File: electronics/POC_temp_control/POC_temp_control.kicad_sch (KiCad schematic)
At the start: 177 parts, among them J1 Conn_01x02, J2 Conn_01x07, J3 Conn_01x05, J4 Conn_01x06, J5 Conn_01x02, J6 Conn_01x02, Q1 PXT8050, Q2 PXT8050, Q3 PXT8550, Q4 Q_PMOS_DUAL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

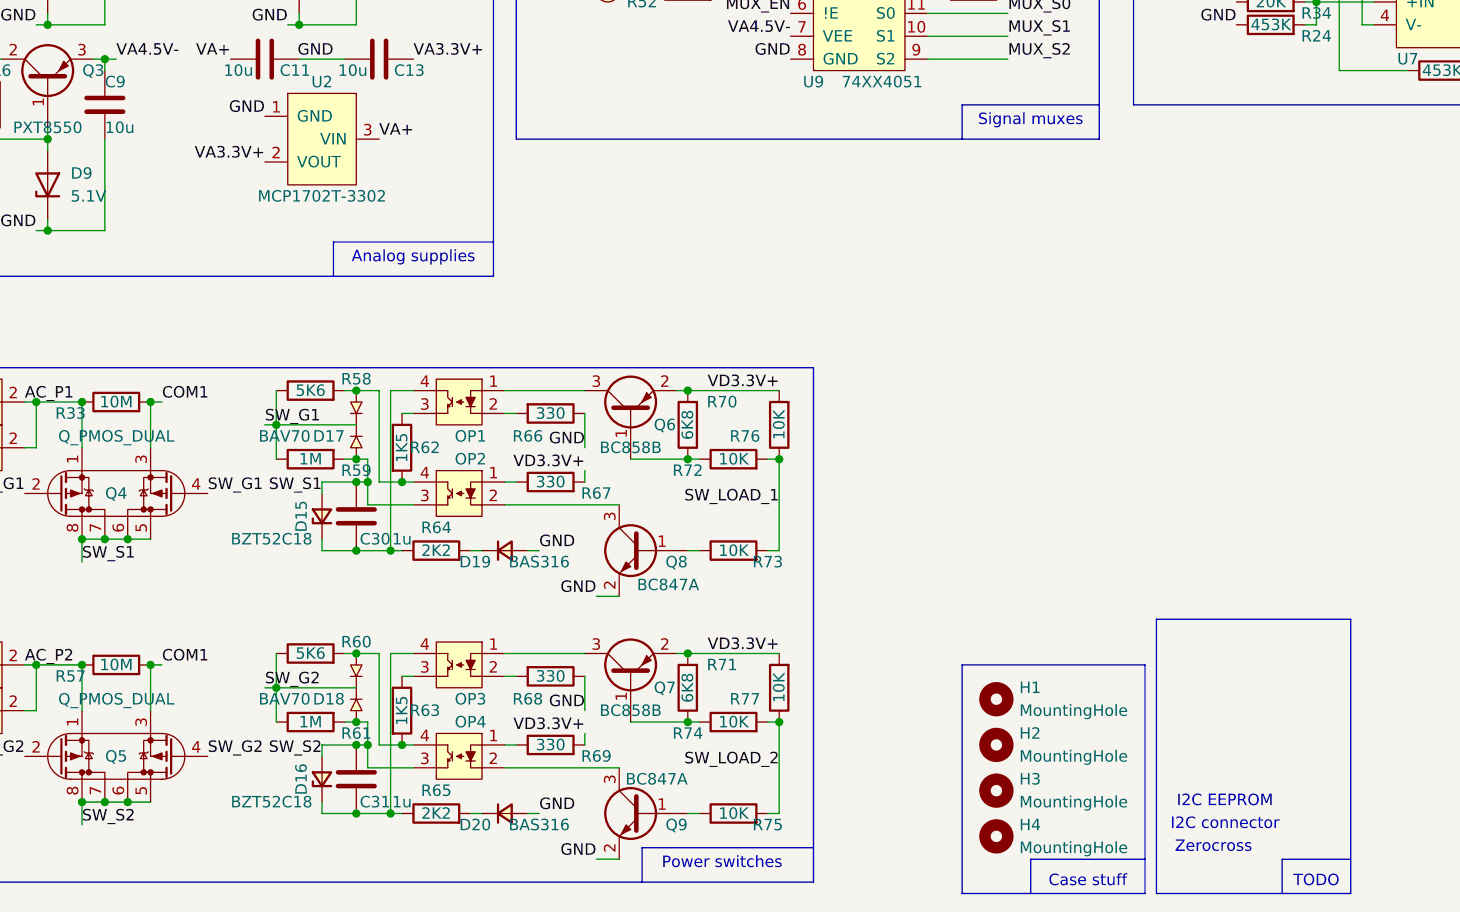
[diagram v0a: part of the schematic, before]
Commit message: added zerocross detector schematic
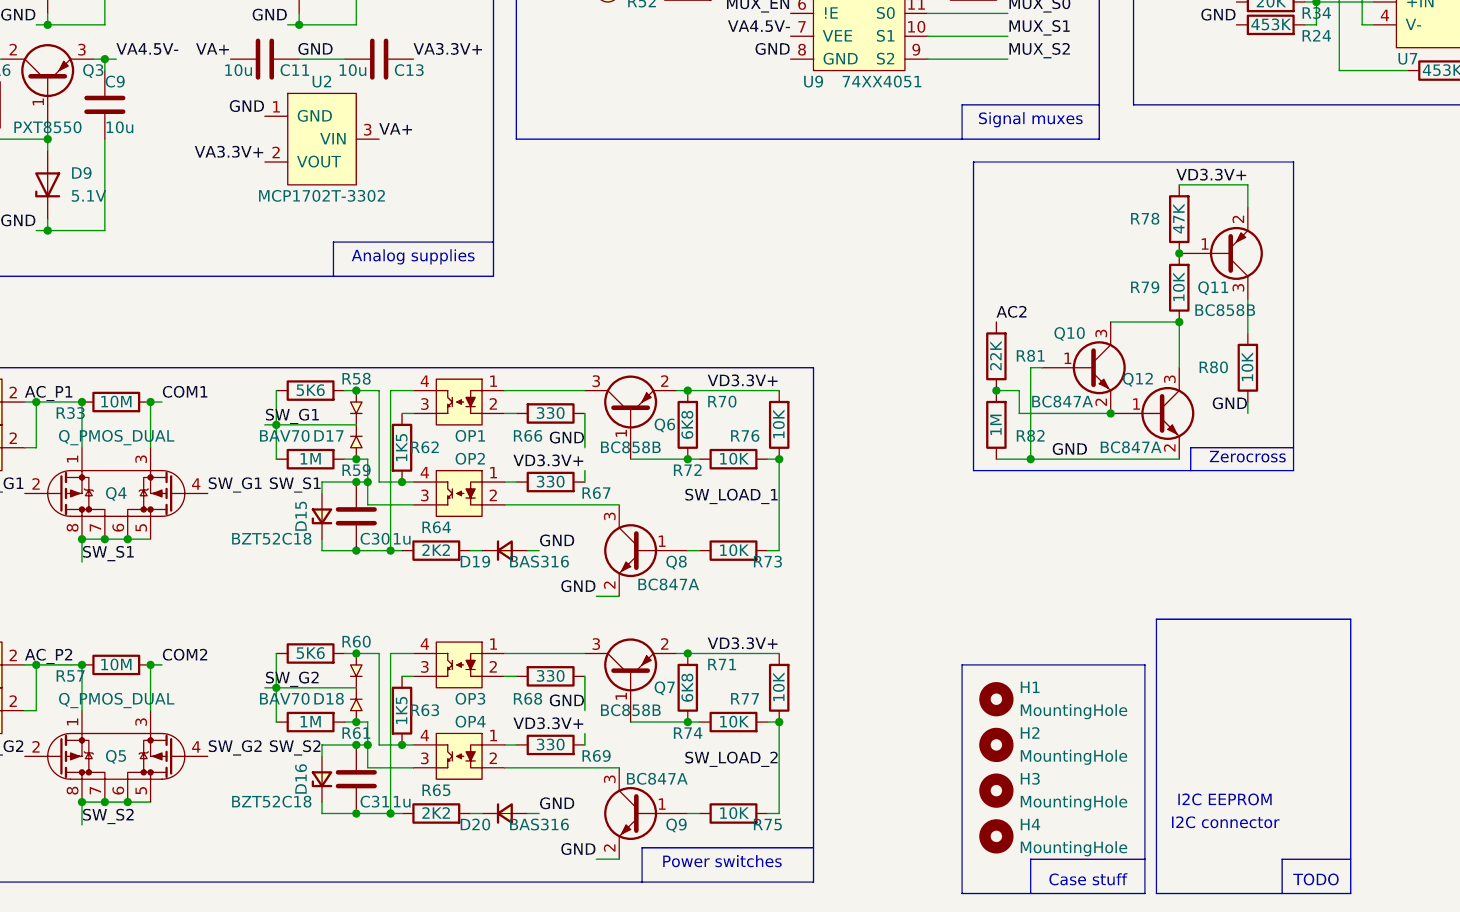
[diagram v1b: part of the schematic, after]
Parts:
- added Q10, Q12: BC847A, SquantorIC:SOT23-3, symbol Device:Q_NPN_BEC
- added Q11: BC858B, SquantorIC:SOT23-3, symbol Device:Q_PNP_BEC
- added R78: 47K, SquantorResistor:R_0603_hand, symbol Device:R
- added R79, R80: 10K, SquantorResistor:R_0603_hand, symbol Device:R
- added R81: 22K, SquantorResistor:R_0603_hand, symbol Device:R
- added R82: 1M, SquantorResistor:R_0603_hand, symbol Device:R
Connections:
- net AC2: now also R81.2
- net COM1: no longer Q5.3 (S2), R57.2
- net COM2: now also Q5.3 (S2), R57.2
- net GND: now also Q10.1 (B), Q12.2 (E), R80.1, R82.1
- net VD3.3V+: now also Q11.2 (E), R78.2
- new net: Q10.2 (E), Q12.1 (B), R81.1, R82.2
- new net: Q10.3 (C), Q12.3 (C), R79.1
- new net: Q11.3 (C), R80.2
- new net: Q11.1 (B), R78.1, R79.2

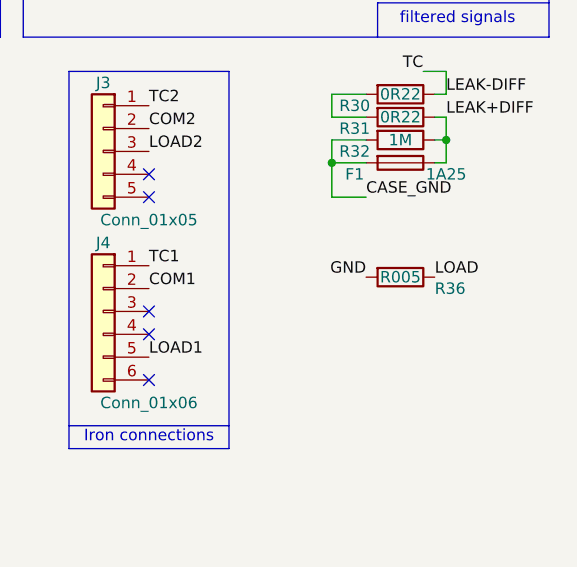
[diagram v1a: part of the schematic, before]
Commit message: replaced current sense resistor, imported zerocross detector
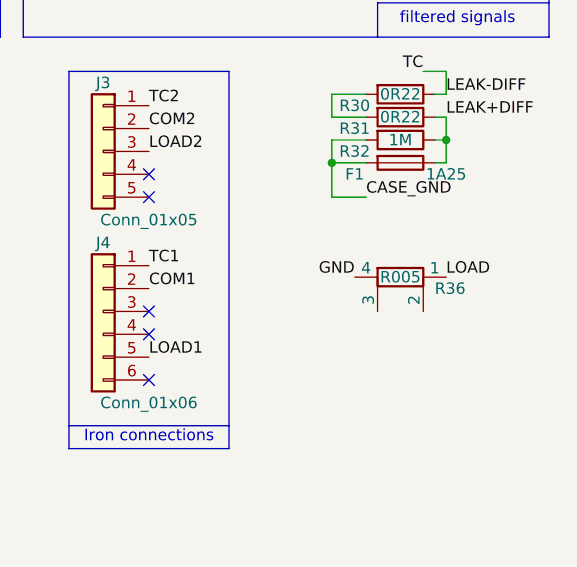
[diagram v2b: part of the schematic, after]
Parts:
- R36: footprint SquantorResistor:R_2512 -> SquantorResistor:R_1225_kelvin; symbol Device:R -> Device:R_Shunt
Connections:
- net GND: now also R36.4; no longer R36.2
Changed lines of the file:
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@@
 	)
 	(label "GND"
-		(at 262.89 135.89 180)
+		(at 261.62 135.89 180)
 		(fields_autoplaced yes)
 		(effects
@@
 	)
 	(label "LOAD"
-		(at 270.51 135.89 0)
+		(at 271.78 135.89 0)
 		(fields_autoplaced yes)
 		(effects
@@
 	)
 	(symbol
-		(lib_id "Device:R")
+		(lib_id "Device:R_Shunt")
 		(at 266.7 135.89 270)
 		(unit 1)
@@
 			)
 		)
-		(property "Footprint" "SquantorResistor:R_2512"
+		(property "Footprint" "SquantorResistor:R_1225_kelvin"
 			(at 266.7 134.112 90)
 			(effects
@@
 			)
 		)
-		(property "Description" "Resistor"
+		(property "Description" "Shunt resistor"
 			(at 266.7 135.89 0)
 			(effects
@@
 		(pin "2"
 		)
+		(pin "4"
+		)
+		(pin "3"
+		)
 		(instances

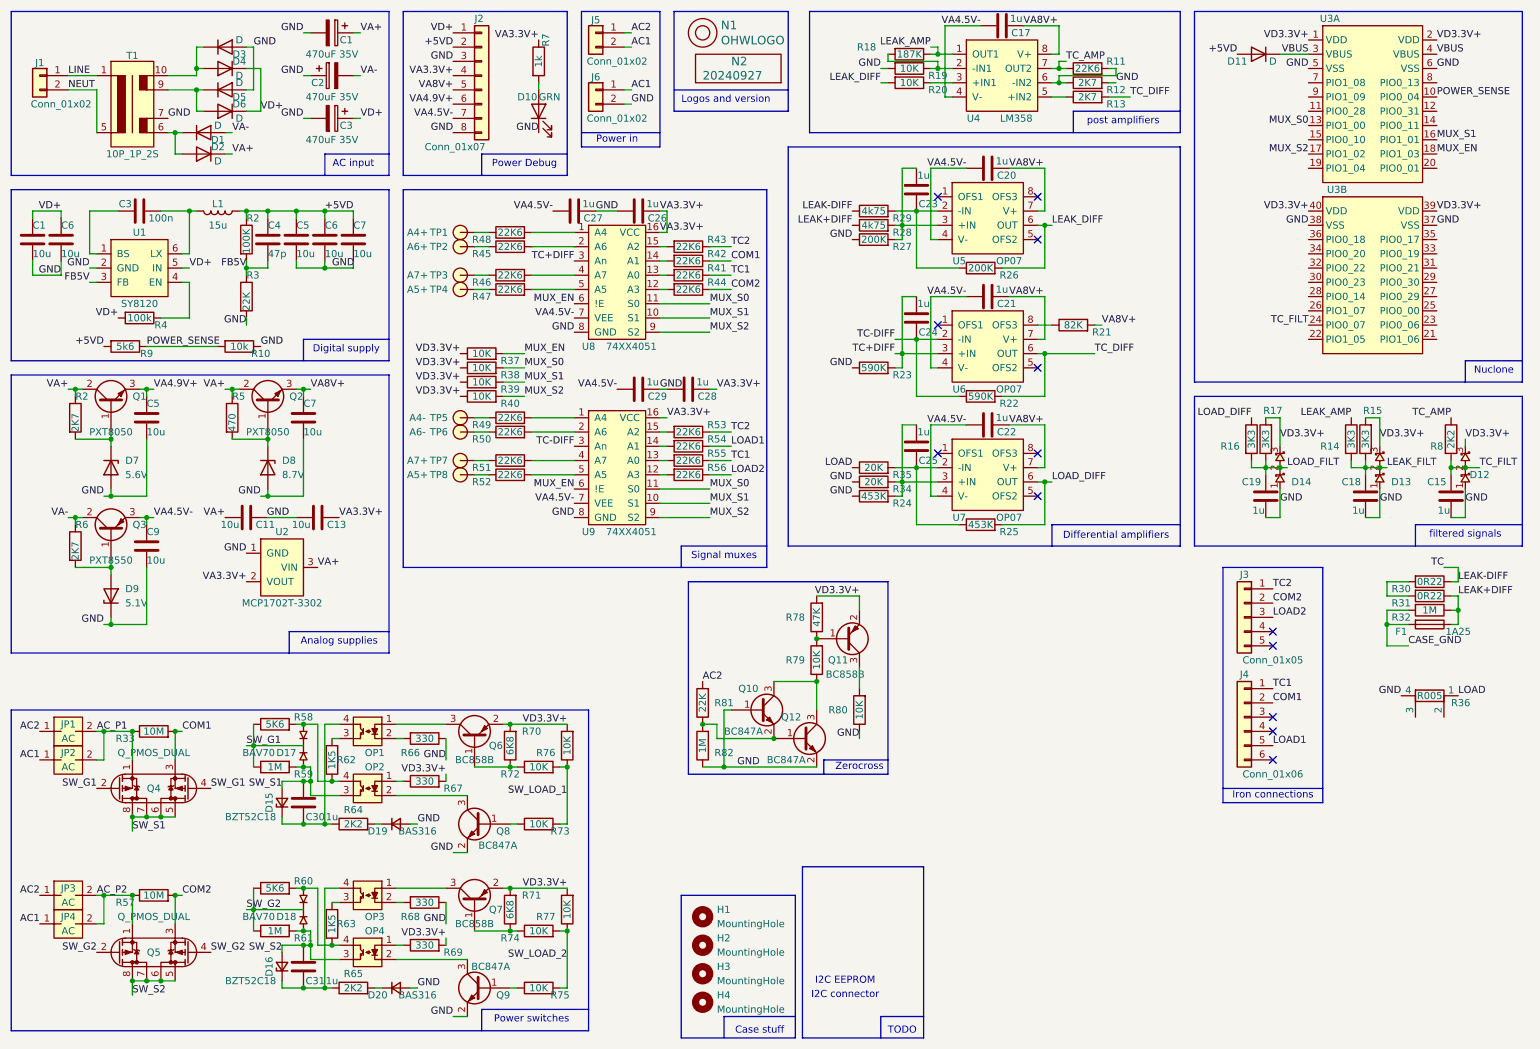
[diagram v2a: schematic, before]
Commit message: more schematic bits added, passes ERC, placing components and fixing silk orientations
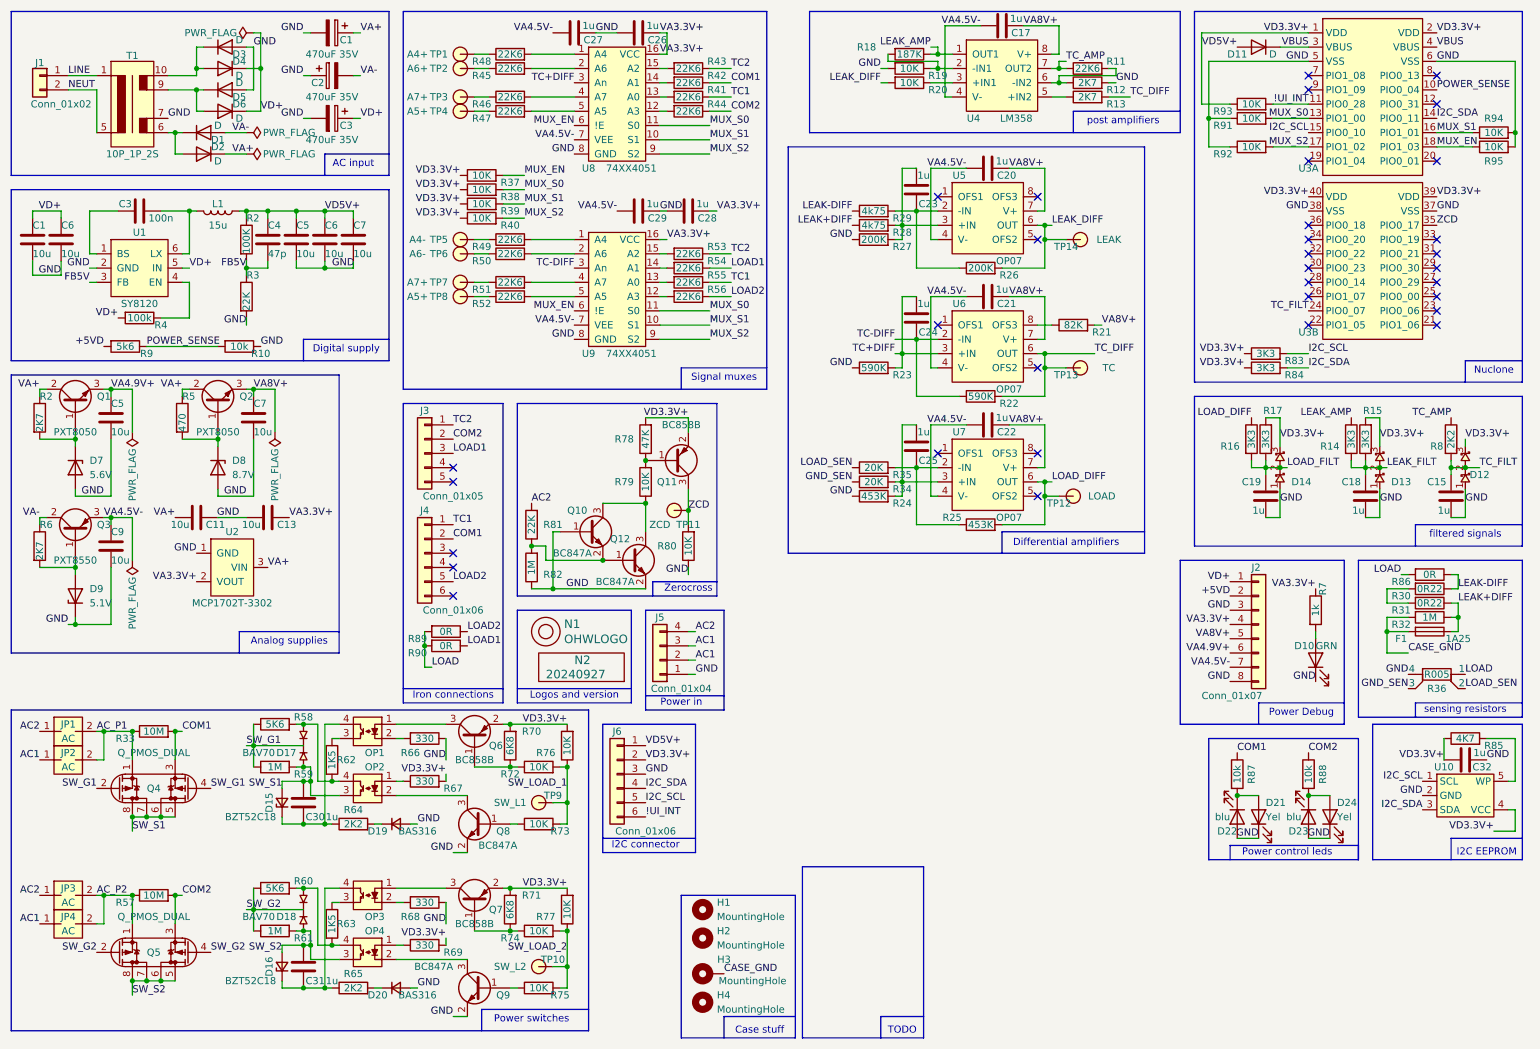
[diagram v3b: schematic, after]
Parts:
- removed J5, J6: Conn_01x02, SquantorPhoenixContact:MKDS_2conn_508pitch_1711725, symbol Connector_Generic:Conn_01x02
- added C32: 1u, SquantorCapacitor:C_0603, symbol Device:C
- added D21, D24: Yel, SquantorDiodes:LED_0603_hand, symbol Device:LED
- added D22, D23: blu, SquantorDiodes:LED_0603_hand, symbol Device:LED
- added J5: Conn_01x04, SquantorConnectors:phoenix-MSTBVA-1755752-4p-508-str, symbol Connector_Generic:Conn_01x04
- added J6: Conn_01x06, Connector_JST:JST_PH_B6B-PH-K_1x06_P2.00mm_Vertical, symbol Connector_Generic:Conn_01x06
- added R83, R84: 3K3, SquantorResistor:R_0603_hand, symbol Device:R
- added R85: 4K7, SquantorResistor:R_0603_hand, symbol Device:R
- added R86, R89, R90: 0R, SquantorResistor:R_1206, symbol Device:R
- added R87, R88: 10k, SquantorResistor:R_0603_hand, symbol Device:R
- added R91, R92, R93, R94, R95: 10K, SquantorResistor:R_0603_hand, symbol Device:R
- added TP10: SW_L2, SquantorTestPoints:TestPoint_hole_H05R10, symbol SquantorProto:testpad
- added TP11: ZCD, SquantorTestPoints:TestPoint_hole_H05R10, symbol SquantorProto:testpad
- added TP12: LOAD, SquantorTestPoints:TestPoint_hole_H05R10, symbol SquantorProto:testpad
- added TP13: TC, SquantorTestPoints:TestPoint_hole_H05R10, symbol SquantorProto:testpad
- added TP14: LEAK, SquantorTestPoints:TestPoint_hole_H05R10, symbol SquantorProto:testpad
- added TP9: SW_L1, SquantorTestPoints:TestPoint_hole_H05R10, symbol SquantorProto:testpad
- added U10: ~, SquantorIC:SOT23-5-Microchip-OT, symbol SquantorGenericDigital:EEPROM_SOT_I2C
- F1: footprint SquantorResistor:R_1206 -> SquantorFuse:FH_XF-155
- H3: symbol Mechanical:MountingHole -> Mechanical:MountingHole_Pad
- R30, R31: footprint SquantorResistor:R_0805+0603 -> SquantorResistor:R_1206
- R36: symbol Device:R_Shunt -> SquantorDevice:R_Shunt
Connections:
- net +5VD: no longer C4.1, C5.1, C6.1, C7.1, D11.2 (A), L1.1, R2.1
- net AC1: now also J5.2 (Pin_2), J5.3 (Pin_3)
- net AC2: now also J5.4 (Pin_4)
- net CASE_GND: now also H3.1
- net COM1: now also R87.1
- net COM2: now also R88.1
- net GND: now also C32.1, D21.1 (K), D22.2 (A), D23.2 (A), D24.1 (K), J5.1 (Pin_1), J6.3 (Pin_3), R91.1, R92.1, R94.2, R95.2, U10.2 (GND); no longer R34.1
- net LEAK-DIFF: now also R86.1
- net LEAK_DIFF: now also TP14.1
- net LOAD: now also R86.2, R89.2, R90.2; no longer R35.1
- net LOAD1: now also J3.3 (Pin_3), R90.1; no longer J4.5 (Pin_5)
- net LOAD2: now also J4.5 (Pin_5), R89.1; no longer J3.3 (Pin_3)
- net LOAD_DIFF: now also TP12.1
- net MUX_EN: now also R95.1
- net MUX_S0: now also R91.2
- net MUX_S1: now also R94.1
- net MUX_S2: now also R92.2
- net SW_LOAD_1: now also TP9.1
- net SW_LOAD_2: now also TP10.1
- net TC_DIFF: now also TP13.1
- net VD3.3V+: now also C32.2, J6.2 (Pin_2), R83.1, R84.1, R85.1, R93.1, U10.4 (VCC)
- net ZCD: now reaches Q11.3 (C), R80.2
- net ZCD: now also U3.35 (PIO0_17), TP11.1
- net !UI_INT: now reaches U3.11 (PIO0_28)
- net !UI_INT: now also J6.6 (Pin_6), R93.2
- net I2C_SDA: now reaches U3.14 (PIO0_11)
- net I2C_SDA: now also J6.4 (Pin_4), R84.2, U10.3 (SDA)
- net I2C_SCL: now reaches U3.15 (PIO0_10)
- net I2C_SCL: now also J6.5 (Pin_5), R83.2, U10.1 (SCL)
- net LOAD_SEN: now reaches R36.2
- net LOAD_SEN: now also R35.1
- net GND_SEN: now reaches R36.3
- net GND_SEN: now also R34.1
- new net: D21.2 (A), D22.1 (K), R87.2
- new net: D23.1 (K), D24.2 (A), R88.2
- new net: R85.2, U10.5 (WP)
- new net VD5V+: C4.1, C5.1, C6.1, C7.1, D11.2 (A), J6.1 (Pin_1), L1.1, R2.1
- no-connect marks 13 -> 33
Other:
- note added: "Power control leds"
- note added: "sensing resistors"
- moved on the sheet: C11, C13, C26, C27, C28, C29, C5, C7, C9, D10, D11, D7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

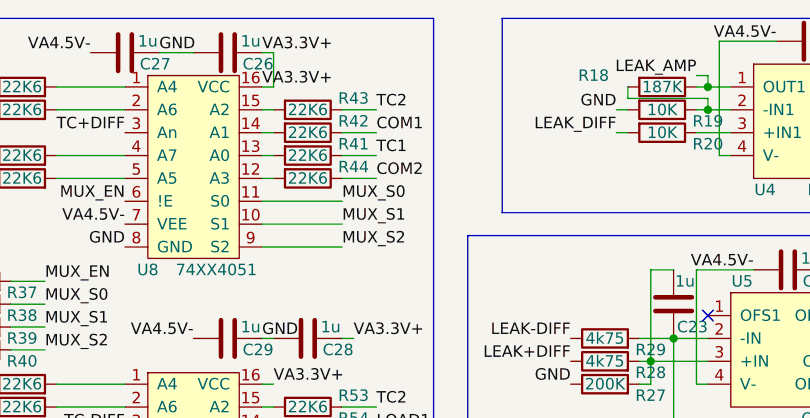
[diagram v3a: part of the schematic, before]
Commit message: some placing and routing done
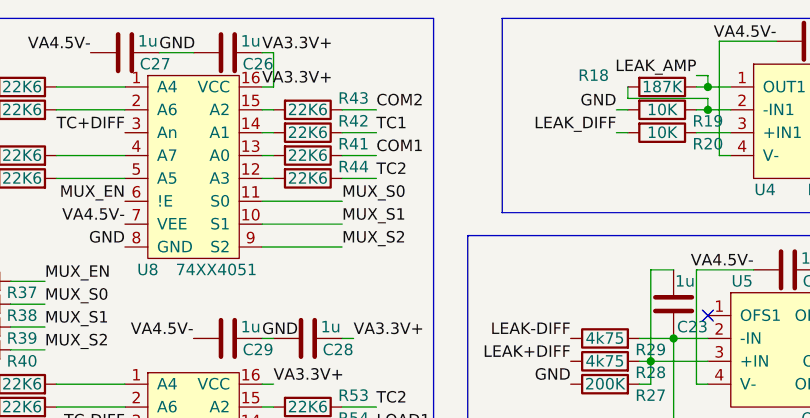
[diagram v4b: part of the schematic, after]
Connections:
- net COM1: now also R41.1; no longer R42.1
- net COM2: now also R43.1; no longer R44.1
- net TC1: now also R42.1; no longer R41.1
- net TC2: now also R44.1; no longer R43.1
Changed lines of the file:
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@@
 	)
 	(label "COM1"
-		(at 142.24 26.67 0)
+		(at 142.24 29.21 0)
 		(fields_autoplaced yes)
 		(effects
@@
 	)
 	(label "COM2"
-		(at 142.24 31.75 0)
+		(at 142.24 24.13 0)
 		(fields_autoplaced yes)
 		(effects
@@
 	)
 	(label "TC2"
-		(at 142.24 24.13 0)
+		(at 142.24 31.75 0)
 		(fields_autoplaced yes)
 		(effects
@@
 	)
 	(label "TC1"
-		(at 142.24 29.21 0)
-		(fields_autoplaced yes)
-		(effects
+		(at 142.24 26.67 0)
+		(fields_autoplaced yes)
+		(effects
